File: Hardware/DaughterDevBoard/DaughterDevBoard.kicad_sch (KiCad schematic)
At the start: 23 parts, among them J1 PS/2, J10 I/O_PWR, J11 DIVIDER, J18 SD_CARD, J2 I/O0, J3 ISA1, J4 ISA0, J5 I/O1, J6 CPU_CLOCK, J7 JOYPAD1, J9 LCD, U1 74HC590A, X1 ACO-20MHz

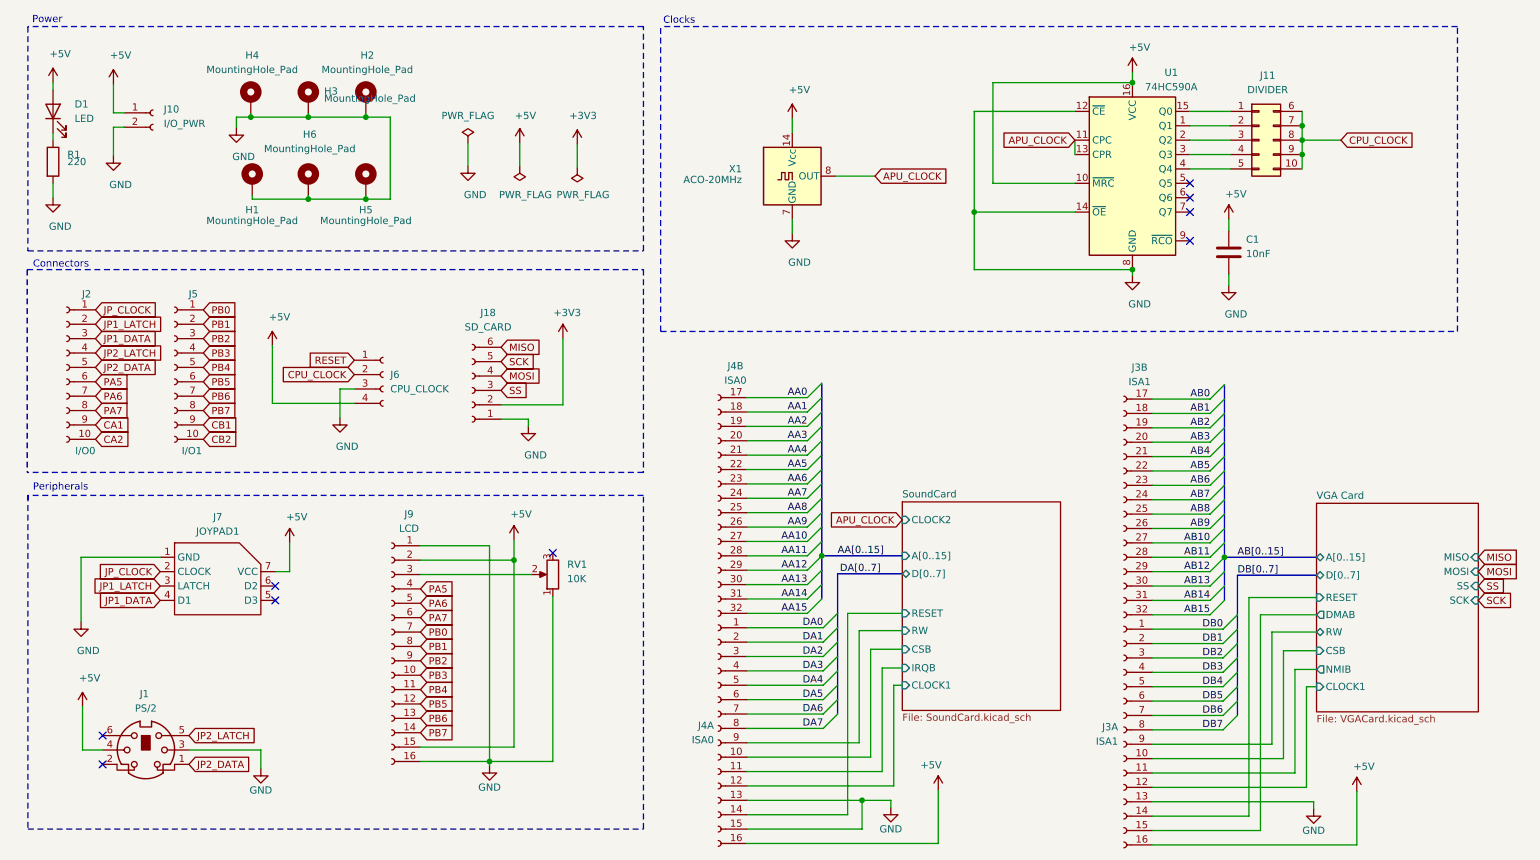
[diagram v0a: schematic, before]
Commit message: Update to Kicad 6.0
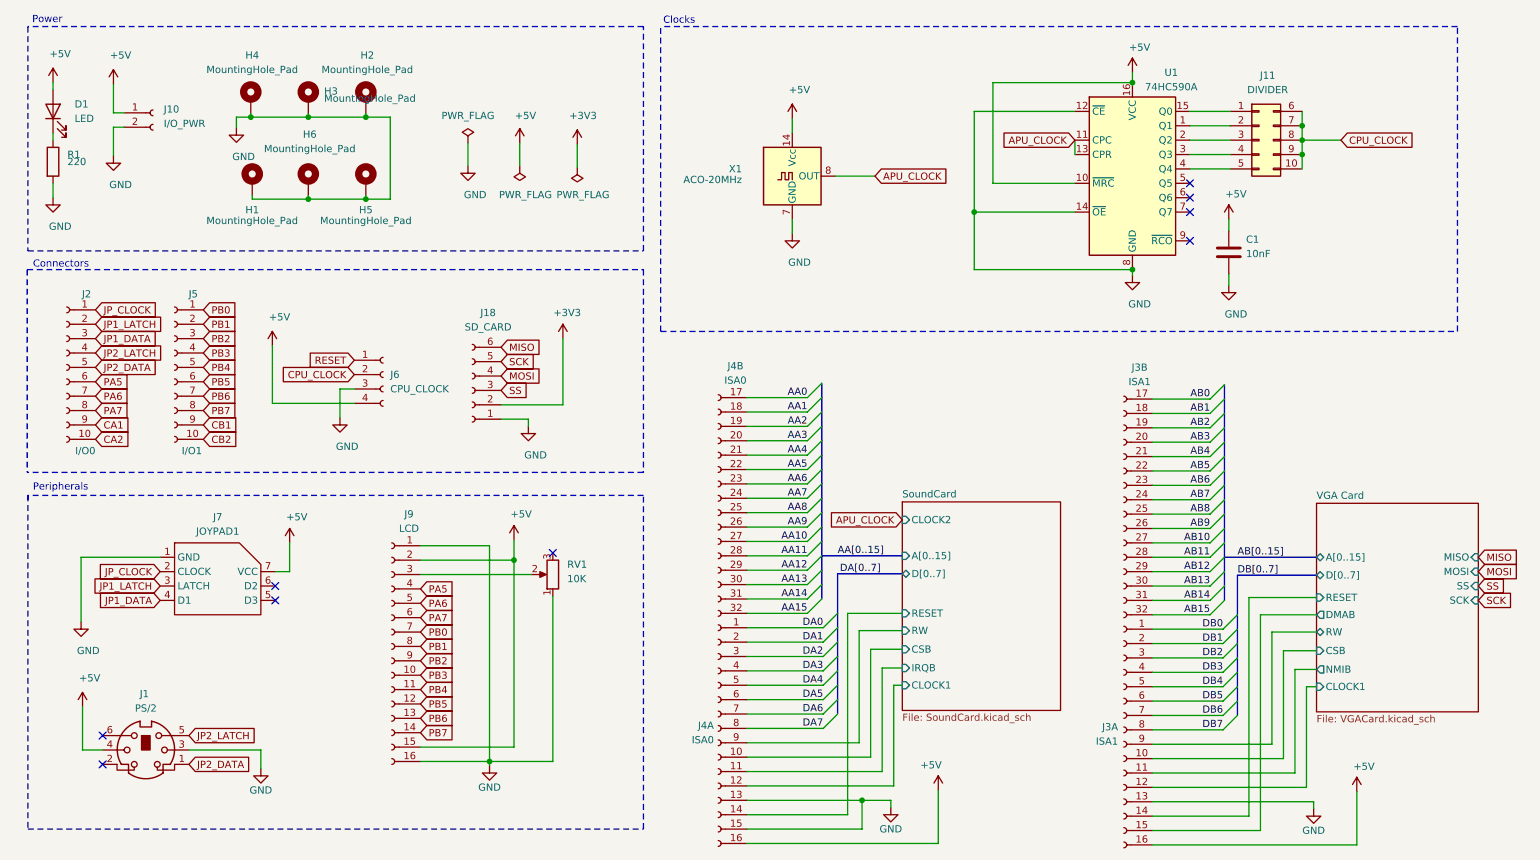
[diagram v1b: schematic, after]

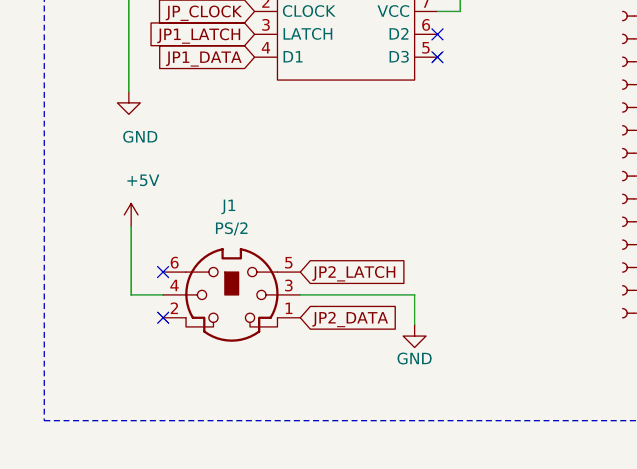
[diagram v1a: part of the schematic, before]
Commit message: Fix Reset, WAI Signal, Add PROG jumper and reformat luc files
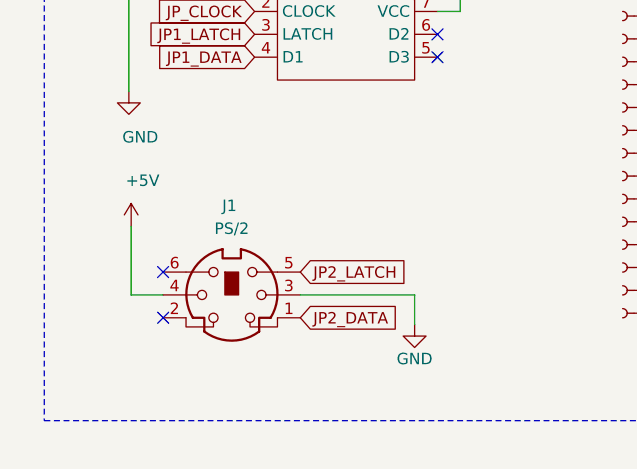
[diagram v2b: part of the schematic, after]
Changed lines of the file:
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@@
       (reference "#PWR018") (unit 1) (value "+5V") (footprint "")
+    )
+    (path "/44b3dba6-c922-4b00-a6a9-2bdfde93ac86/cd158472-09e9-4d28-b5c9-17f0928cbaaa"
+      (reference "#PWR019") (unit 1) (value "+5V") (footprint "")
+    )
+    (path "/44b3dba6-c922-4b00-a6a9-2bdfde93ac86/92c81e5f-030a-4a7c-9ca0-f77e1407f440"
+      (reference "#PWR020") (unit 1) (value "+3V3") (footprint "")
+    )
+    (path "/44b3dba6-c922-4b00-a6a9-2bdfde93ac86/57f0a2a8-d5b4-4093-a0ea-8a738524097e"
+      (reference "#PWR021") (unit 1) (value "+5V") (footprint "")
+    )
+    (path "/44b3dba6-c922-4b00-a6a9-2bdfde93ac86/200f4a61-7f4d-4d5e-a57a-c28835635b66"
+      (reference "#PWR022") (unit 1) (value "GND") (footprint "")
+    )
+    (path "/44b3dba6-c922-4b00-a6a9-2bdfde93ac86/69836d19-1237-4fac-8aea-7c34d48cd3c4"
+      (reference "#PWR023") (unit 1) (value "+3V3") (footprint "")
+    )
+    (path "/44b3dba6-c922-4b00-a6a9-2bdfde93ac86/5a9a2985-b3f0-41f0-82f7-cc7e9b5ff033"
+      (reference "#PWR024") (unit 1) (value "GND") (footprint "")
     )
     (path "/60791882-3d6e-4a3e-b50b-871010120b90"
@@
       (reference "C17") (unit 1) (value "100nF") (footprint "Capacitor_SMD:C_0603_1608Metric")
     )
+    (path "/44b3dba6-c922-4b00-a6a9-2bdfde93ac86/3c611489-9240-4d21-b3e2-63a4fa91d256"
+      (reference "C18") (unit 1) (value "100nF") (footprint "Capacitor_SMD:C_0603_1608Metric")
+    )
+    (path "/44b3dba6-c922-4b00-a6a9-2bdfde93ac86/923e3bc1-ca9f-41a5-b2e6-ec5d0ee654eb"
+      (reference "C19") (unit 1) (value "100nF") (footprint "Capacitor_SMD:C_0603_1608Metric")
+    )
     (path "/e28705fe-a84e-4931-82de-894472437d2f"
       (reference "D1") (unit 1) (value "LED") (footprint "LED_THT:LED_D5.0mm")
@@
       (reference "J7") (unit 1) (value "JOYPAD1") (footprint "Connector_TheRLab:NES_JoyPad")
     )
+    (path "/44b3dba6-c922-4b00-a6a9-2bdfde93ac86/ac6db401-00fb-401c-a75a-8456969119b4"
+      (reference "J8") (unit 1) (value "PROG") (footprint "Connector_PinHeader_2.54mm:PinHeader_1x02_P2.54mm_Vertical")
+    )
     (path "/5bcefb22-3248-4e04-bc31-6a6a74f3c1f9"
       (reference "J9") (unit 1) (value "LCD") (footprint "Connector_PinSocket_2.54mm:PinSocket_1x16_P2.54mm_Vertical")
@@
       (reference "R8") (unit 1) (value "680") (footprint "Resistor_THT:R_Axial_DIN0207_L6.3mm_D2.5mm_P10.16mm_Horizontal")
     )
-    (path "/44b3dba6-c922-4b00-a6a9-2bdfde93ac86/0dc17f29-9ba4-43d0-a126-c78351ff3400"
-      (reference "R9") (unit 1) (value "2K2") (footprint "Resistor_THT:R_Axial_DIN0207_L6.3mm_D2.5mm_P10.16mm_Horizontal")
-    )
-    (path "/44b3dba6-c922-4b00-a6a9-2bdfde93ac86/5a269c62-2fa5-4581-8aba-d160fb132b67"
-      (reference "R10") (unit 1) (value "3K3") (footprint "Resistor_THT:R_Axial_DIN0207_L6.3mm_D2.5mm_P10.16mm_Horizontal")
-    )
     (path "/211b6312-de19-406c-adb6-eab41604df41"
       (reference "RV1") (unit 1) (value "10K") (footprint "Potentiometer_THT:Potentiometer_Bourns_3266Y_Vertical")
@@
       (reference "U4") (unit 1) (value "SN74LVC2T45QDCURQ1") (footprint "Package_SO:VSSOP-8_2.3x2mm_P0.5mm")
     )
-    (path "/44b3dba6-c922-4b00-a6a9-2bdfde93ac86/0dc061c7-833e-4f16-a892-25ba624f9c0d"
-      (reference "U5") (unit 1) (value "SN74LVC2T45QDCURQ1") (footprint "Package_SO:VSSOP-8_2.3x2mm_P0.5mm")
+    (path "/44b3dba6-c922-4b00-a6a9-2bdfde93ac86/66b754b9-f2ce-439e-8065-37e9ee79f971"
+      (reference "U5") (unit 1) (value "SN74LVC1T45DCK") (footprint "Package_TO_SOT_SMD:SOT-363_SC-70-6")
     )
     (path "/44b3dba6-c922-4b00-a6a9-2bdfde93ac86/7438e7b3-8bcf-4f11-8561-cafbc54c8465"
@@
       (reference "U8") (unit 1) (value "SN74LVC8T245DBQR") (footprint "Package_SO:TSSOP-24_4.4x7.8mm_P0.65mm")
     )
+    (path "/44b3dba6-c922-4b00-a6a9-2bdfde93ac86/7ed0ad05-6e81-49bd-9492-84b73054710a"
+      (reference "U9") (unit 1) (value "SN74LVC1T45DCK") (footprint "Package_TO_SOT_SMD:SOT-363_SC-70-6")
+    )
     (path "/b7972eeb-816c-4046-adcb-be79e50f379e"

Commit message: Add monostable to reset PPU
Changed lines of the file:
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@@
       (reference "#PWR018") (unit 1) (value "+5V") (footprint "")
     )
-    (path "/44b3dba6-c922-4b00-a6a9-2bdfde93ac86/cd158472-09e9-4d28-b5c9-17f0928cbaaa"
+    (path "/44b3dba6-c922-4b00-a6a9-2bdfde93ac86/eccbfed2-2734-4b2c-a804-89706842bdf5"
       (reference "#PWR019") (unit 1) (value "+5V") (footprint "")
     )
-    (path "/44b3dba6-c922-4b00-a6a9-2bdfde93ac86/92c81e5f-030a-4a7c-9ca0-f77e1407f440"
-      (reference "#PWR020") (unit 1) (value "+3V3") (footprint "")
-    )
-    (path "/44b3dba6-c922-4b00-a6a9-2bdfde93ac86/57f0a2a8-d5b4-4093-a0ea-8a738524097e"
-      (reference "#PWR021") (unit 1) (value "+5V") (footprint "")
-    )
-    (path "/44b3dba6-c922-4b00-a6a9-2bdfde93ac86/200f4a61-7f4d-4d5e-a57a-c28835635b66"
+    (path "/44b3dba6-c922-4b00-a6a9-2bdfde93ac86/9e108a1d-e2c6-4afe-b0ee-2a5668858a28"
+      (reference "#PWR020") (unit 1) (value "GND") (footprint "")
+    )
+    (path "/44b3dba6-c922-4b00-a6a9-2bdfde93ac86/dbefb299-d923-422c-97fc-44d315659a37"
+      (reference "#PWR021") (unit 1) (value "+3.3V") (footprint "")
+    )
+    (path "/44b3dba6-c922-4b00-a6a9-2bdfde93ac86/4ffacb6f-db51-4e6f-9006-4be2617fa73c"
       (reference "#PWR022") (unit 1) (value "GND") (footprint "")
-    )
-    (path "/44b3dba6-c922-4b00-a6a9-2bdfde93ac86/69836d19-1237-4fac-8aea-7c34d48cd3c4"
-      (reference "#PWR023") (unit 1) (value "+3V3") (footprint "")
-    )
-    (path "/44b3dba6-c922-4b00-a6a9-2bdfde93ac86/5a9a2985-b3f0-41f0-82f7-cc7e9b5ff033"
-      (reference "#PWR024") (unit 1) (value "GND") (footprint "")
     )
     (path "/60791882-3d6e-4a3e-b50b-871010120b90"
@@
       (reference "#PWR0134") (unit 1) (value "GND") (footprint "")
     )
-    (path "/44b3dba6-c922-4b00-a6a9-2bdfde93ac86/a733d02f-b41e-49a8-b4d8-16dc8475e1f1"
-      (reference "#PWR0135") (unit 1) (value "GND") (footprint "")
-    )
     (path "/44b3dba6-c922-4b00-a6a9-2bdfde93ac86/54dd7e0c-6eda-452b-8466-0eebfc59c3ab"
       (reference "#PWR0136") (unit 1) (value "GND") (footprint "")
@@
       (reference "C17") (unit 1) (value "100nF") (footprint "Capacitor_SMD:C_0603_1608Metric")
     )
-    (path "/44b3dba6-c922-4b00-a6a9-2bdfde93ac86/3c611489-9240-4d21-b3e2-63a4fa91d256"
-      (reference "C18") (unit 1) (value "100nF") (footprint "Capacitor_SMD:C_0603_1608Metric")
-    )
-    (path "/44b3dba6-c922-4b00-a6a9-2bdfde93ac86/923e3bc1-ca9f-41a5-b2e6-ec5d0ee654eb"
-      (reference "C19") (unit 1) (value "100nF") (footprint "Capacitor_SMD:C_0603_1608Metric")
+    (path "/44b3dba6-c922-4b00-a6a9-2bdfde93ac86/24f5d115-7545-4571-b63c-0b647e65c09d"
+      (reference "C18") (unit 1) (value "100uF") (footprint "")
+    )
+    (path "/44b3dba6-c922-4b00-a6a9-2bdfde93ac86/6a0a59b9-bbf9-43b8-ad98-380cde3b1911"
+      (reference "C19") (unit 1) (value "10nF") (footprint "Capacitor_THT:C_Disc_D5.0mm_W2.5mm_P2.50mm")
+    )
+    (path "/44b3dba6-c922-4b00-a6a9-2bdfde93ac86/b6a361aa-e021-4ebe-bb70-6a610f474f9d"
+      (reference "C20") (unit 1) (value "100uF") (footprint "")
     )
     (path "/e28705fe-a84e-4931-82de-894472437d2f"
@@
       (reference "J18") (unit 1) (value "SD_CARD") (footprint "Connector_PinSocket_2.54mm:PinSocket_1x06_P2.54mm_Vertical")
     )
+    (path "/44b3dba6-c922-4b00-a6a9-2bdfde93ac86/28342419-733a-44b4-b39d-76ab80270121"
+      (reference "Q1") (unit 1) (value "2N2222A") (footprint "digikey-footprints:TO-18-3")
+    )
     (path "/f0708b6a-7f3b-4253-a8dc-8ed0958b62d5"
       (reference "R1") (unit 1) (value "220") (footprint "Resistor_THT:R_Axial_DIN0207_L6.3mm_D2.5mm_P10.16mm_Horizontal")
@@
       (reference "R8") (unit 1) (value "680") (footprint "Resistor_THT:R_Axial_DIN0207_L6.3mm_D2.5mm_P10.16mm_Horizontal")
     )
+    (path "/44b3dba6-c922-4b00-a6a9-2bdfde93ac86/3ce287c0-66f6-4bd1-b1c8-d5d8c7dc8725"
+      (reference "R9") (unit 1) (value "2.2K") (footprint "Resistor_THT:R_Axial_DIN0207_L6.3mm_D2.5mm_P10.16mm_Horizontal")
+    )
+    (path "/44b3dba6-c922-4b00-a6a9-2bdfde93ac86/1ed6c3d5-b74c-42c1-918b-d972787a6b79"
+      (reference "R10") (unit 1) (value "1K") (footprint "Resistor_THT:R_Axial_DIN0207_L6.3mm_D2.5mm_P10.16mm_Horizontal")
+    )
+    (path "/44b3dba6-c922-4b00-a6a9-2bdfde93ac86/ada1a5c5-2d23-42fb-be94-5eae99bcb591"
+      (reference "R11") (unit 1) (value "10K") (footprint "Resistor_THT:R_Axial_DIN0207_L6.3mm_D2.5mm_P10.16mm_Horizontal")
+    )
     (path "/211b6312-de19-406c-adb6-eab41604df41"
       (reference "RV1") (unit 1) (value "10K") (footprint "Potentiometer_THT:Potentiometer_Bourns_3266Y_Vertical")
@@
       (reference "U4") (unit 1) (value "SN74LVC2T45QDCURQ1") (footprint "Package_SO:VSSOP-8_2.3x2mm_P0.5mm")
     )
-    (path "/44b3dba6-c922-4b00-a6a9-2bdfde93ac86/66b754b9-f2ce-439e-8065-37e9ee79f971"
-      (reference "U5") (unit 1) (value "SN74LVC1T45DCK") (footprint "Package_TO_SOT_SMD:SOT-363_SC-70-6")
+    (path "/44b3dba6-c922-4b00-a6a9-2bdfde93ac86/c7cd7e41-05d6-4c93-bfa1-439f1c2b93ee"
+      (reference "U5") (unit 1) (value "NE555P") (footprint "digikey-footprints:DIP-8_W7.62mm")
     )
     (path "/44b3dba6-c922-4b00-a6a9-2bdfde93ac86/7438e7b3-8bcf-4f11-8561-cafbc54c8465"

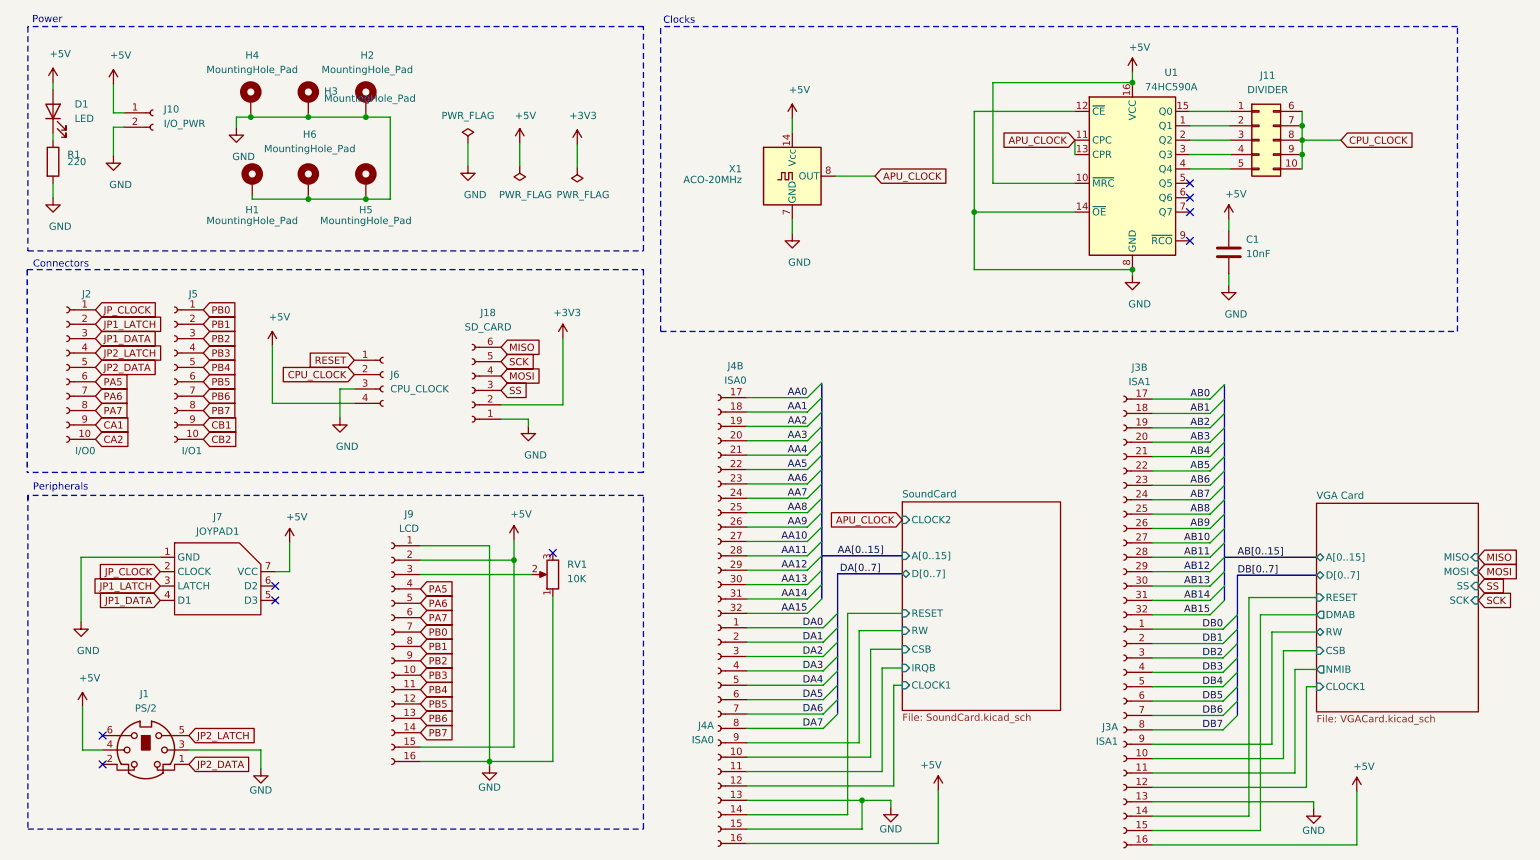
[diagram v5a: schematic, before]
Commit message: Remove Alchitry shield
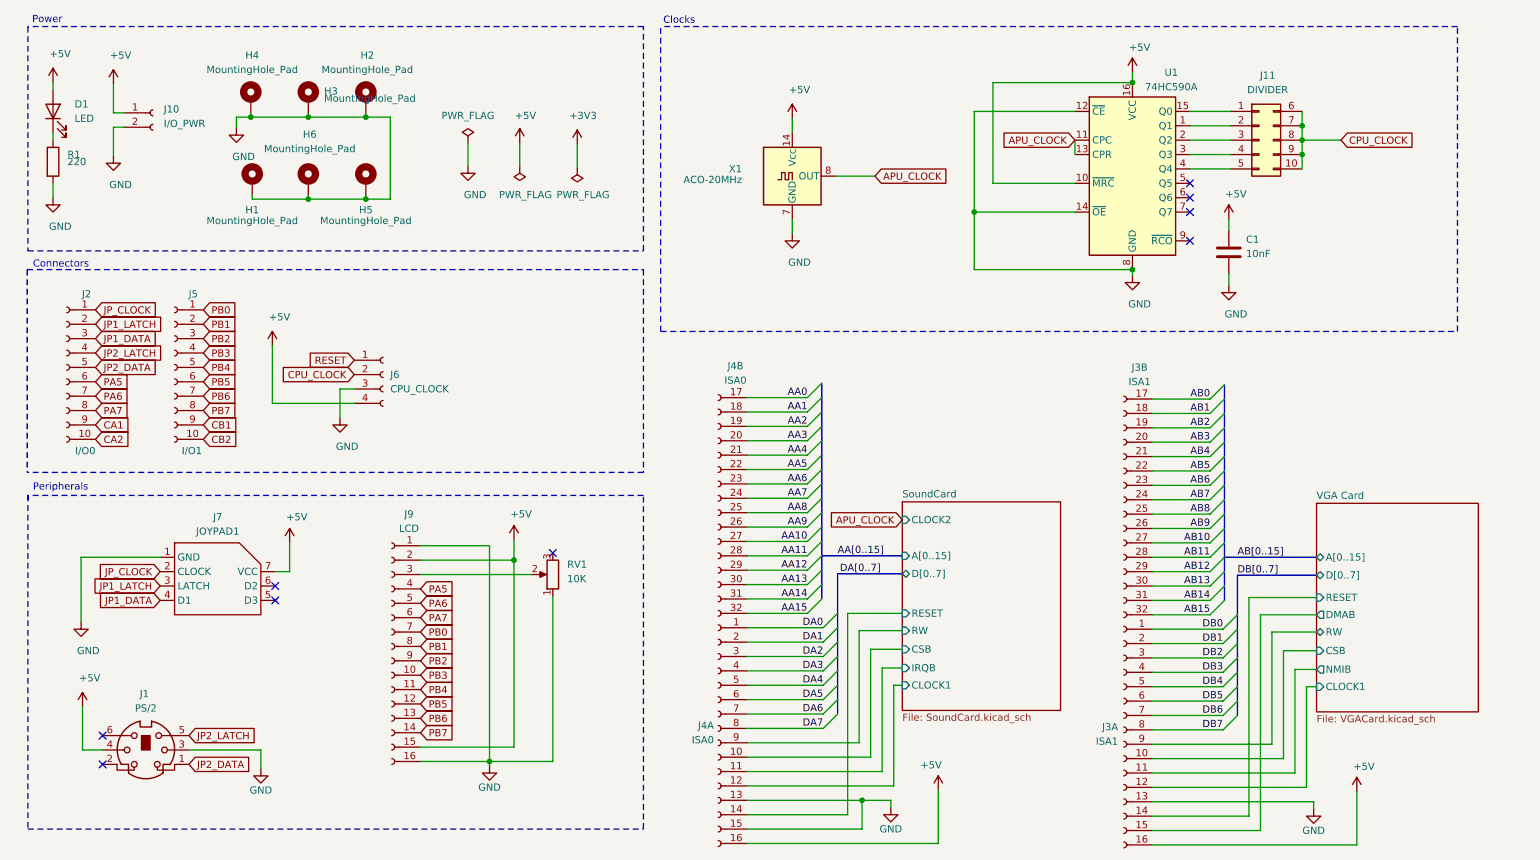
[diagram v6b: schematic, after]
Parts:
- removed J18: SD_CARD, Connector_PinSocket_2.54mm:PinSocket_1x06_P2.54mm_Vertical, symbol Connector:Conn_01x06_Female
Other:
- sheet VGA Card ports: added none; removed MISO, MOSI, SCK, SS
